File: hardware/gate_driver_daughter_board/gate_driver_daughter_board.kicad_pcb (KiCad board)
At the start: 2 copper layers, 0 parts

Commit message: PCBrev1
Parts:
- added C1: 1000uF, gate_driver_daughter_board:25V1000uF, F.Cu at (115.9, 39.3)
- added C10: 1uF, Capacitor_SMD:C_0805_2012Metric_Pad1.18x1.45mm_HandSolder, F.Cu at (156.0, 117.3)
- added C11: 0.1uF, Capacitor_SMD:C_0805_2012Metric_Pad1.18x1.45mm_HandSolder, F.Cu at (114.1, 83.7)
- added C12: 100nF, Capacitor_SMD:C_0805_2012Metric_Pad1.18x1.45mm_HandSolder, F.Cu at (173.2, 116.6)
- added C13: 10uF, Capacitor_SMD:C_0805_2012Metric_Pad1.18x1.45mm_HandSolder, F.Cu at (170.7, 116.6)
- added C14: 1000uF, gate_driver_daughter_board:25V1000uF, F.Cu at (172.8, 44.9)
- added C15: 0.1uF, Capacitor_SMD:C_0805_2012Metric_Pad1.18x1.45mm_HandSolder, F.Cu at (128.5, 81.3)
- added C16: 1000uF, gate_driver_daughter_board:25V1000uF, F.Cu at (150.6, 37.1)
- added C17: 1000uF, gate_driver_daughter_board:25V1000uF, F.Cu at (161.6, 44.9)
- added C18: 0.33uF, Capacitor_SMD:C_0805_2012Metric_Pad1.18x1.45mm_HandSolder, F.Cu at (154.9, 51.1)
- added C19: 10uF, Capacitor_SMD:C_0805_2012Metric_Pad1.18x1.45mm_HandSolder, F.Cu at (149.9, 45.2)
- added C2: 0.1uF, Capacitor_SMD:C_0805_2012Metric_Pad1.18x1.45mm_HandSolder, F.Cu at (106.7, 51.8)
- added C20: 1uF, Capacitor_SMD:C_0805_2012Metric_Pad1.18x1.45mm_HandSolder, F.Cu at (152.5, 45.2)
- added C21: 100nF, Capacitor_SMD:C_0805_2012Metric_Pad1.18x1.45mm_HandSolder, F.Cu at (155.0, 45.2)
- added C22: 0.1uF, Capacitor_SMD:C_0805_2012Metric_Pad1.18x1.45mm_HandSolder, F.Cu at (154.9, 56.1)
- added C23: 0.1uF, Capacitor_SMD:C_0805_2012Metric_Pad1.18x1.45mm_HandSolder, F.Cu at (138.2, 80.8)
- added C24: 10nF, Capacitor_SMD:C_0805_2012Metric_Pad1.18x1.45mm_HandSolder, F.Cu at (149.4, 86.4)
- added C25: 47nF, Capacitor_SMD:C_0805_2012Metric_Pad1.18x1.45mm_HandSolder, F.Cu at (154.4, 84.3)
- added C26: 0.1uF, Capacitor_SMD:C_0805_2012Metric_Pad1.18x1.45mm_HandSolder, F.Cu at (155.4, 76.7)
- added C27: 0.33uF, Capacitor_SMD:C_0805_2012Metric_Pad1.18x1.45mm_HandSolder, F.Cu at (114.8, 51.8)
- added C28: 0.1uF, Capacitor_SMD:C_0805_2012Metric_Pad1.18x1.45mm_HandSolder, F.Cu at (114.8, 55.9)
- added C3: 1000uF, gate_driver_daughter_board:25V1000uF, F.Cu at (104.7, 39.3)
- added C4: 1000uF, gate_driver_daughter_board:25V1000uF, F.Cu at (104.6, 33.3)
- added C5: 2.2uF, Capacitor_SMD:C_0805_2012Metric_Pad1.18x1.45mm_HandSolder, F.Cu at (106.7, 55.9)
- added C6: 10uF, Capacitor_SMD:C_0805_2012Metric_Pad1.18x1.45mm_HandSolder, F.Cu at (117.4, 33.5)
- added C7: 1uF, Capacitor_SMD:C_0805_2012Metric_Pad1.18x1.45mm_HandSolder, F.Cu at (114.9, 33.5)
- added C8: 100nF, Capacitor_SMD:C_0805_2012Metric_Pad1.18x1.45mm_HandSolder, F.Cu at (120.0, 33.5)
- added C9: 100nF, Capacitor_SMD:C_0805_2012Metric_Pad1.18x1.45mm_HandSolder, F.Cu at (153.4, 117.3)
- added H1: GATE, gate_driver_daughter_board:MountingHole_4.3x6.2mm_M4_Pad, F.Cu at (189.0, 115.4)
- added H2: EMITTER, gate_driver_daughter_board:MountingHole_4.3x6.2mm_M4_Pad, F.Cu at (176.0, 75.6)
- added J1: Conn_01x08, Connector_Molex:Molex_Nano-Fit_105309-xx08_1x08_P2.50mm_Vertical, F.Cu at (105.1, 76.8)
- added J2: Conn_01x02, Connector_Molex:Molex_Nano-Fit_105309-xx02_1x02_P2.50mm_Vertical, F.Cu at (152.6, 65.7)
- added J3: Conn_01x02, Connector_Molex:Molex_Nano-Fit_105309-xx02_1x02_P2.50mm_Vertical, F.Cu at (105.1, 99.8)
- added JP1: Jumper_2_Small_Open, Connector_PinHeader_2.54mm:PinHeader_1x02_P2.54mm_Vertical, F.Cu at (175.3, 107.2)
- added JP2: Jumper_2_Small_Open, Connector_PinHeader_2.54mm:PinHeader_1x02_P2.54mm_Vertical, F.Cu at (181.4, 109.7)
- added R1: R?, Resistor_SMD:R_1206_3216Metric_Pad1.30x1.75mm_HandSolder, F.Cu at (153.4, 109.2)
- added R10: 1k, Resistor_SMD:R_0805_2012Metric_Pad1.20x1.40mm_HandSolder, F.Cu at (138.2, 84.8)
- added R11: 154k, Resistor_SMD:R_0805_2012Metric_Pad1.20x1.40mm_HandSolder, F.Cu at (141.2, 74.2)
- added R12: 10k, Resistor_SMD:R_0805_2012Metric_Pad1.20x1.40mm_HandSolder, F.Cu at (137.7, 73.2)
- added R13: 8.87k, Resistor_SMD:R_0805_2012Metric_Pad1.20x1.40mm_HandSolder, F.Cu at (137.7, 75.2)
- added R14: 8.2k, Resistor_SMD:R_0805_2012Metric_Pad1.20x1.40mm_HandSolder, F.Cu at (151.9, 84.3)
- added R15: 6.8k, Resistor_SMD:R_0805_2012Metric_Pad1.20x1.40mm_HandSolder, F.Cu at (149.4, 82.3)
- added R16: 6.8k, Resistor_SMD:R_0805_2012Metric_Pad1.20x1.40mm_HandSolder, F.Cu at (151.9, 80.3)
- added R17: 10k, Resistor_SMD:R_0805_2012Metric_Pad1.20x1.40mm_HandSolder, F.Cu at (145.3, 75.2)
- added R18: 10k, Resistor_SMD:R_0805_2012Metric_Pad1.20x1.40mm_HandSolder, F.Cu at (145.3, 73.2)
- added R19: 100k, Resistor_SMD:R_0805_2012Metric_Pad1.20x1.40mm_HandSolder, F.Cu at (145.3, 115.3)
- added R3: 2.2k, Resistor_SMD:R_0805_2012Metric_Pad1.20x1.40mm_HandSolder, F.Cu at (114.6, 80.1)
- added R4: 360, Resistor_SMD:R_0805_2012Metric_Pad1.20x1.40mm_HandSolder, F.Cu at (128.5, 83.8)
- added R5: 102k, Resistor_SMD:R_0805_2012Metric_Pad1.20x1.40mm_HandSolder, F.Cu at (128.5, 78.7)
- added R6: 976k, Resistor_SMD:R_0805_2012Metric_Pad1.20x1.40mm_HandSolder, F.Cu at (130.6, 75.9)
- added R7: 130k 0.5%, Resistor_SMD:R_0805_2012Metric_Pad1.20x1.40mm_HandSolder, F.Cu at (133.6, 78.2)
- added R8: R?, Resistor_SMD:R_1206_3216Metric_Pad1.30x1.75mm_HandSolder, F.Cu at (179.8, 116.3)
- added R9: R?, Resistor_SMD:R_1206_3216Metric_Pad1.30x1.75mm_HandSolder, F.Cu at (179.8, 113.3)
- added Rg1: 549, Resistor_SMD:R_0805_2012Metric_Pad1.20x1.40mm_HandSolder, F.Cu at (151.4, 69.1)
- added TP1: InAmp_Bias/Amp, TestPoint:TestPoint_Pad_D3.0mm, F.Cu at (141.2, 88.4)
- added TP2: InAmp_Filtered, TestPoint:TestPoint_Pad_D3.0mm, F.Cu at (145.8, 88.4)
- added TP3: InAmpOut, TestPoint:TestPoint_Pad_2.0x2.0mm, F.Cu at (154.7, 80.5)
- added U1: LF33_TO220, Package_TO_SOT_THT:TO-220-3_Vertical, F.Cu at (109.8, 50.8)
- added U2: REC20K-2412SZ, gate_driver_daughter_board:REC20K_RCP, F.Cu at (124.4, 36.6)
- added U3: 6N137, Package_DIP:DIP-8_W7.62mm, F.Cu at (125.0, 86.2)
- added U4: NCD57100DWR2G, Package_SO:SOIC-16W_7.5x10.3mm_P1.27mm, F.Cu at (163.1, 112.4)
- added U5: LTC6992CS6-2-TRMPBF, Package_TO_SOT_SMD:TSOT-23-6, F.Cu at (133.6, 81.3)
- added U6: LM7805_TO220, Package_TO_SOT_THT:TO-220-3_Vertical, F.Cu at (149.9, 50.5)
- added U7: MCP6004, Package_SO:SOIC-14_3.9x8.7mm_P1.27mm, F.Cu at (143.8, 81.3)
- added U8: INA826, Package_SO:SOIC-8_3.9x4.9mm_P1.27mm, F.Cu at (151.3, 74.2)
- added U9: LM7805_TO220, Package_TO_SOT_THT:TO-220-3_Vertical, F.Cu at (117.9, 50.8)
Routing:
- net +15V_Isolated: track 0.00 -> 134.1 mm
- net +12V: track 0.00 -> 123.2 mm
- net +5V_Isolated: track 0.00 -> 106.2 mm
- net +3.3V: track 0.00 -> 100.3 mm, vias 0 -> 4
- net /~{Rp_GD_ResetFinal}: track 0.00 -> 87.1 mm
- net /Rp_GD_Ready: track 0.00 -> 63.6 mm
- net /~{Rp_GD_Fault}: track 0.00 -> 63.2 mm
- net /Rb_GateDrive: track 0.00 -> 57.0 mm
- net +5V: track 0.00 -> 37.2 mm, vias 0 -> 1
- net Net-(JP2-A): track 0.00 -> 26.8 mm
- net Net-(U7B--): track 0.00 -> 23.9 mm, vias 0 -> 2
- net Net-(U7B-+): track 0.00 -> 16.6 mm
- net Net-(U5-MOD): track 0.00 -> 14.4 mm
- net /Rp_CurrentSense: track 0.00 -> 12.6 mm
- net Net-(U4-OUTH): track 0.00 -> 11.9 mm
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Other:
- board outline added: 103.9 x 116.8 mm

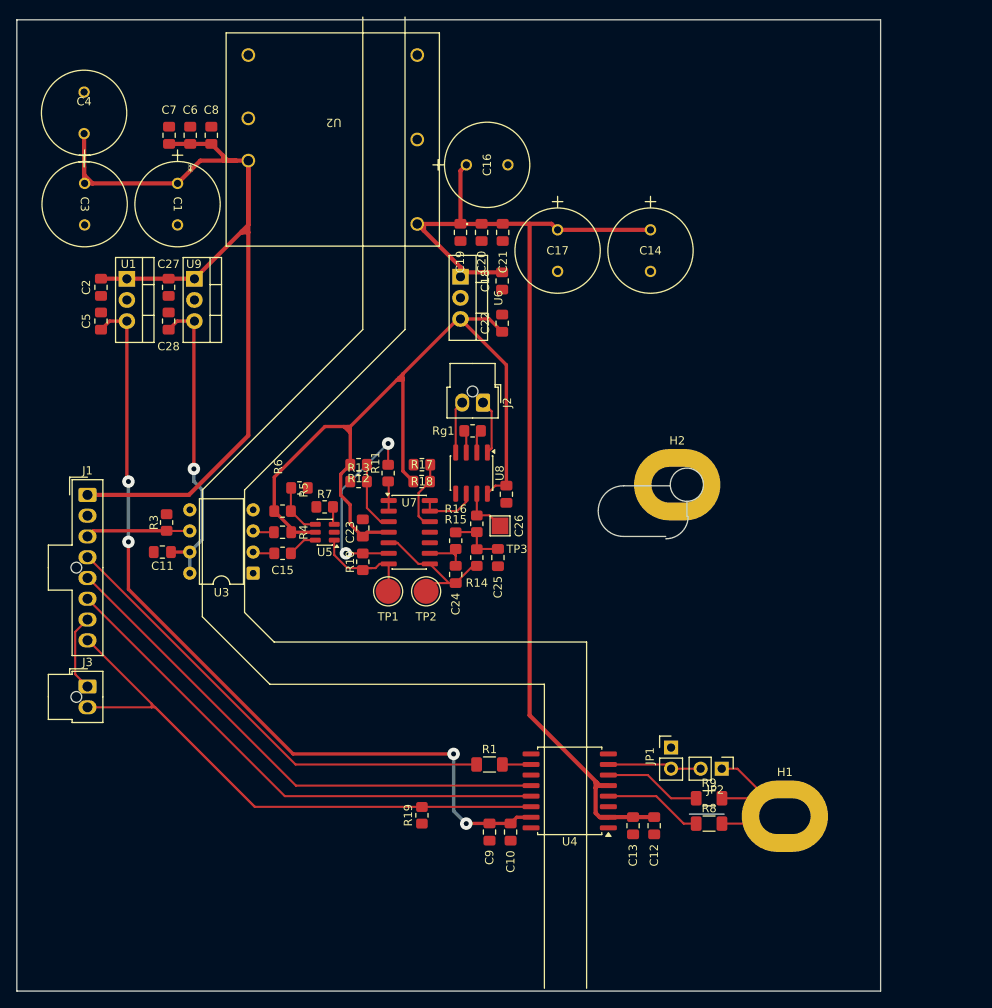
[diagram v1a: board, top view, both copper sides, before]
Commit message: Add Isolation Keepout Zone, little bit of ground routing
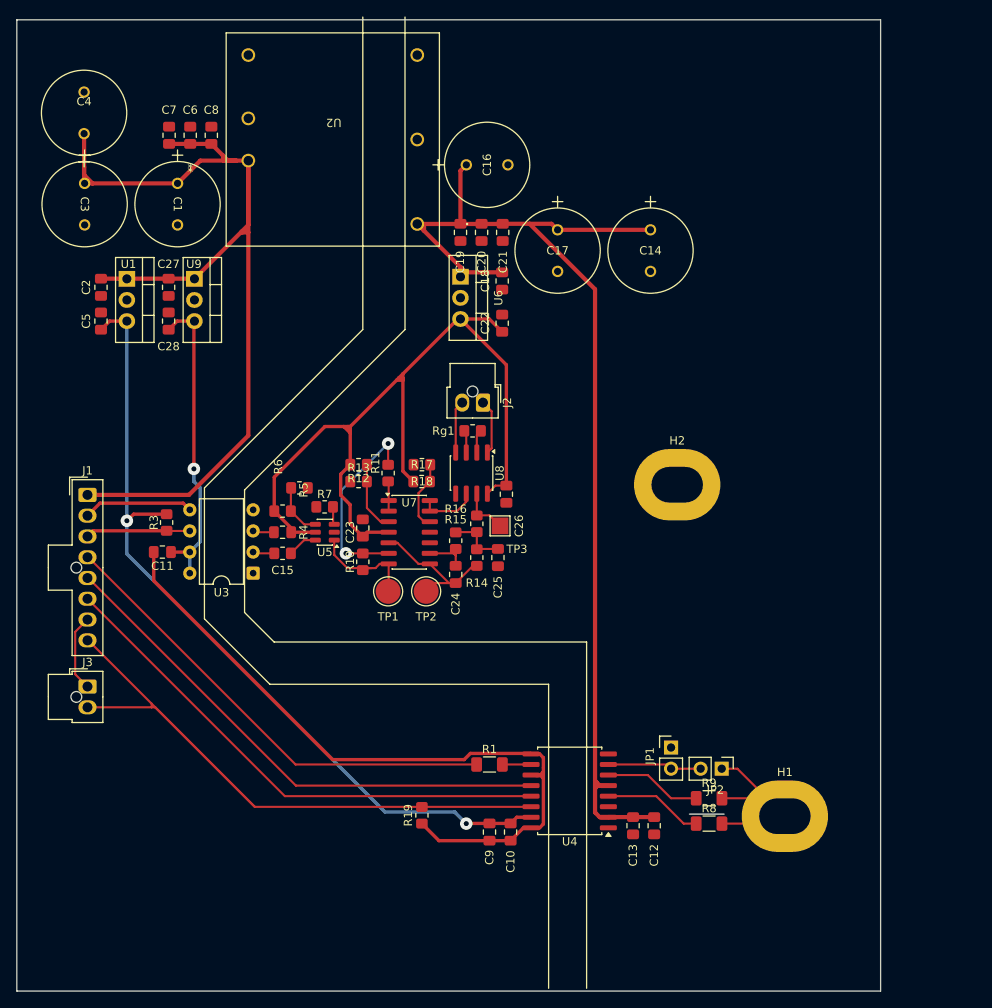
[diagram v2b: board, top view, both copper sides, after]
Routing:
- net GND: track 0.00 -> 100.7 mm
- net +3.3V: track 100.3 -> 99.2 mm, vias 4 -> 2
- net +15V_Isolated: track 134.1 -> 134.9 mm
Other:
- outline, holes or cut-outs redrawn

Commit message: Annular Ring Adjustment
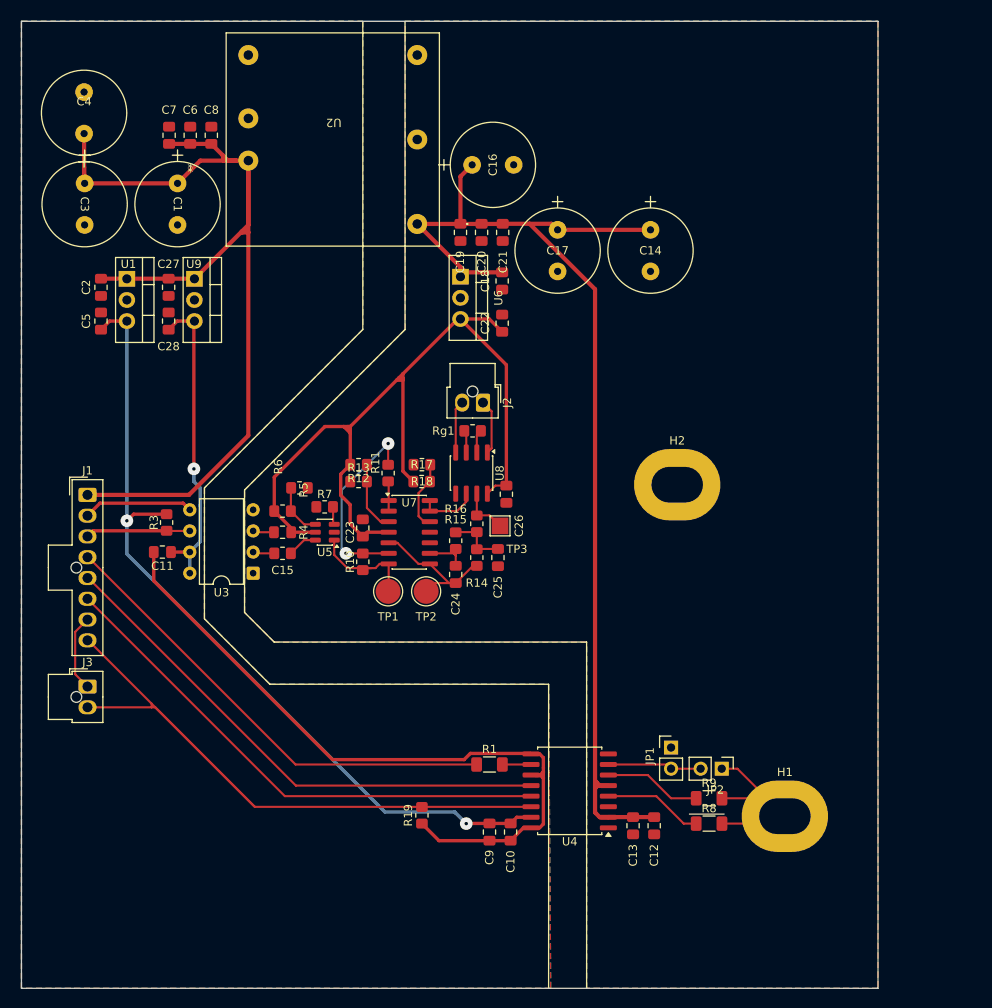
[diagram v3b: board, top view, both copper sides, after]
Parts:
- moved C16 0.70 mm to (151.3, 37.1)
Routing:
- added copper zone on B.Cu, net Battery-
- added copper zone on F.Cu, net Battery-
- added copper zone on B.Cu, net GND
- added copper zone on F.Cu, net GND
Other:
- board size 103.9 x 116.8 mm -> 103 x 116.3 mm
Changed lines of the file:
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@@
 		(pad "1" thru_hole circle
 			(at 0 0 180)
-			(size 1.651 1.651)
+			(size 2.413 1.651)
 			(drill 1.143)
 			(layers "*.Cu" "*.Mask")
@@
 		(pad "2" thru_hole circle
 			(at 0 5.08 180)
-			(size 1.651 1.651)
+			(size 2.413 1.651)
 			(drill 1.143)
 			(layers "*.Cu" "*.Mask")
@@
 		(pad "3" thru_hole circle
 			(at 0 12.7 180)
-			(size 1.651 1.651)
+			(size 2.413 1.651)
 			(drill 1.143)
 			(layers "*.Cu" "*.Mask")
@@
 		(pad "4" thru_hole circle
 			(at -20.32 12.7 180)
-			(size 1.651 1.651)
+			(size 2.413 1.651)
 			(drill 1.143)
 			(layers "*.Cu" "*.Mask")
@@
 		(pad "5" thru_hole circle
 			(at -20.32 2.54 180)
-			(size 1.651 1.651)
+			(size 2.413 2.413)
 			(drill 1.143)
 			(layers "*.Cu" "*.Mask")
@@
 		(pad "6" thru_hole circle
 			(at -20.32 -7.62 180)
-			(size 1.651 1.651)
+			(size 2.413 1.651)
 			(drill 1.143)
 			(layers "*.Cu" "*.Mask")
@@
 	(footprint "gate_driver_daughter_board:25V1000uF"
 		(layer "F.Cu")
-		(at 150.63275 37.084)
+		(at 151.32875 37.084)
 		(tags "UVY1E102MPD1TD ")
 		(property "Reference" "C16"
@@
 		(pad "1" thru_hole circle
 			(at 0 0)
-			(size 1.3716 1.3716)
+			(size 2.1336 2.1336)
 			(drill 0.8636)
 			(layers "*.Cu" "*.Mask")
@@
 		(pad "2" thru_hole circle
 			(at 5 0)
-			(size 1.3716 1.3716)
+			(size 2.1336 1.3716)
 			(drill 0.8636)
 			(layers "*.Cu" "*.Mask")
@@
 		(pad "1" thru_hole circle
 			(at 0 0 90)
-			(size 1.3716 1.3716)
+			(size 2.1336 1.3716)
 			(drill 0.8636)
 			(layers "*.Cu" "*.Mask")
@@
 		(pad "2" thru_hole circle
 			(at 5 0 90)
-			(size 1.3716 1.3716)
+			(size 2.1336 1.3716)
 			(drill 0.8636)
 			(layers "*.Cu" "*.Mask")
@@
 		(pad "1" thru_hole circle
 			(at 0 0 270)
-			(size 1.3716 1.3716)
+			(size 2.1336 1.3716)
 			(drill 0.8636)
 			(layers "*.Cu" "*.Mask")
@@
 		(pad "2" thru_hole circle
 			(at 5 0 270)
-			(size 1.3716 1.3716)
+			(size 2.1336 1.3716)
 			(drill 0.8636)
 			(layers "*.Cu" "*.Mask")
@@
 		(pad "1" thru_hole circle
 			(at 0 0 270)
-			(size 1.3716 1.3716)
+			(size 2.1336 1.3716)
 			(drill 0.8636)
 			(layers "*.Cu" "*.Mask")
@@
 		(pad "2" thru_hole circle
 			(at 5 0 270)
-			(size 1.3716 1.3716)
+			(size 2.1336 1.3716)
 			(drill 0.8636)
 			(layers "*.Cu" "*.Mask")
@@
 		(pad "1" thru_hole circle
 			(at 0 0 270)
-			(size 1.3716 1.3716)
+			(size 2.1336 1.3716)
 			(drill 0.8636)
 			(layers "*.Cu" "*.Mask")
@@
 		(pad "2" thru_hole circle
 			(at 5 0 270)
-			(size 1.3716 1.3716)
+			(size 2.1336 1.3716)
 			(drill 0.8636)
 			(layers "*.Cu" "*.Mask")
@@
 		(pad "1" thru_hole circle
 			(at 0 0 270)
-			(size 1.3716 1.3716)
+			(size 2.1336 1.3716)
 			(drill 0.8636)
 			(layers "*.Cu" "*.Mask")
@@
 		(pad "2" thru_hole circle
 			(at 5 0 270)
-			(size 1.3716 1.3716)
+			(size 2.1336 1.3716)
 			(drill 0.8636)
 			(layers "*.Cu" "*.Mask")
@@
 	)
 	(gr_line
-		(start 138.176 19.304)
+		(start 138.176 19.812)
 		(end 138.176 56.896)
 		(stroke
@@
 	(gr_line
 		(start 143.256 56.896)
-		(end 143.256 19.304)
+		(end 143.256 19.812)
 		(stroke
 			(width 0.1)
@@
 	)
 	(gr_rect
-		(start 96.557401 19.637365)
-		(end 200.467717 136.477364)
+		(start 97.111468 19.812)
+		(end 200.152 136.143999)
 		(stroke
 			(width 0.05)
@@
 	(via
 		(at 117.856 73.66)
-		(size 1.50114)
-		(drill 0.59944)
+		(size 1.524)
+		(drill 0.4064)
 		(layers "F.Cu" "B.Cu")
 		(net "+5V")
@@
 	(via
 		(at 136.144 83.82)
-		(size 1.50114)
-		(drill 0.59944)
+		(size 1.524)
+		(drill 0.4064)
 		(layers "F.Cu" "B.Cu")
 		(net "Net-(U7B--)")
@@
 	(via
 		(at 141.224 70.612)
-		(size 1.503223)
-		(drill 0.59944)
+		(size 1.524)
+		(drill 0.4064)
 		(layers "F.Cu" "B.Cu")
 		(net "Net-(U7B--)")
@@
 	)
 	(segment
+		(start 149.926 38.48675)
+		(end 151.32875 37.084)
+		(width 0.508)
+		(layer "F.Cu")
+		(net "+15V_Isolated")
+	)
+	(segment
 		(start 166.2775 111.3445)
 		(end 166.116 111.183)
@@
 	)
 	(segment
-		(start 166.439 111.76)
-		(end 166.185 112.014)
+		(start 149.926 44.1745)
+		(end 149.926 38.48675)
 		(width 0.508)
 		(layer "F.Cu")
@@
 	)
 	(segment
-		(start 155.006 44.1745)
-		(end 158.242 44.1745)
-		(width 0.508)
-		(layer "F.Cu")
-		(net "+15V_Isolated")
-	)
-	(segment
-		(start 149.926 37.79075)
-		(end 149.926 44.1745)
+		(start 166.439 111.76)
+		(end 166.185 112.014)
 		(width 0.508)
 		(layer "F.Cu")
@@
 	)
 	(segment
-		(start 150.63275 37.084)
-		(end 149.926 37.79075)
+		(start 155.006 44.1745)
+		(end 158.242 44.1745)
 		(width 0.508)
 		(layer "F.Cu")
@@
 	(via
 		(at 109.794 79.90123)
-		(size 1.50114)
-		(drill 0.59944)
+		(size 1.524)
+		(drill 0.4064)
 		(layers "F.Cu" "B.Cu")
 		(net "+3.3V")
@@
 	(via
 		(at 150.622 116.332)
-		(size 1.50114)
-		(drill 0.59944)
+		(size 1.524)
+		(drill 0.4064)
 		(layers "F.Cu" "B.Cu")
 		(net "+3.3V")
@@
 		(polygon
 			(pts
-				(xy 138.176 19.558) (xy 143.256 19.558) (xy 143.256 56.896) (xy 123.952 76.2) (xy 123.952 90.932)
-				(xy 127.508 94.488) (xy 165.1 94.488) (xy 165.1 136.652) (xy 160.528 136.652) (xy 160.528 99.568)
+				(xy 138.176 19.812) (xy 143.256 19.812) (xy 143.256 56.896) (xy 123.952 76.2) (xy 123.952 90.932)
+				(xy 127.508 94.488) (xy 165.1 94.488) (xy 165.1 136.144) (xy 160.528 136.144) (xy 160.528 99.568)
 				(xy 127 99.568) (xy 119.126 91.694) (xy 119.126 75.946) (xy 138.176 56.896)
 			)
 		)
+	)
+	(zone
+		(net "GND")
+		(layers "F.Cu" "B.Cu")
+		(name "GND")
+		(hatch edge 0.5)
+		(priority 1)
+		(connect_pads yes
+			(clearance 0.4064)
+		)
+		(min_thickness 0.25)
+		(fill yes
+			(thermal_gap 0.5)
+			(thermal_bridge_width 0.5)
+			(island_removal_mode 0)
+		)
+		(polygon
+			(pts
+				(xy 97.111468 19.812) (xy 138.176 19.812) (xy 138.176 56.896) (xy 119.126 75.946) (xy 119.126 91.694)
+				(xy 127 99.568) (xy 160.528 99.568) (xy 160.782 136.144) (xy 97.111468 136.143999)
+			)
+		)
+	)
+	(zone
+		(net "Battery-")
+		(layers "F.Cu" "B.Cu")
+		(name "Bat-")
+		(hatch edge 0.5)
+		(connect_pads yes
+			(clearance 0.4064)
+		)
+		(min_thickness 0.25)
+		(fill yes
+			(thermal_gap 0.5)
+			(thermal_bridge_width 0.5)
+			(island_removal_mode 0)
+		)
+		(polygon
+			(pts
+				(xy 143.256 19.812) (xy 200.152 19.812) (xy 200.152 136.143999) (xy 165.1 136.144) (xy 165.1 94.488)
+				(xy 127.508 94.488) (xy 123.952 90.932) (xy 123.952 76.2) (xy 143.256 56.896)
+			)
+		)

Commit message: V1.0 PCB Ready to Mill, Gate Driver Daughter Board
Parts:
- moved R13 1.59 mm to (138.9, 74.2), turned to -90 degrees
- moved C12 1.55 mm to (173.0, 118.1)
- moved C13 1.55 mm to (170.4, 118.1)
- moved R12 1.44 mm to (136.7, 74.2), turned to 90 degrees
- moved R7 1.00 mm to (132.6, 78.2)
- turned C23 to 90 degrees
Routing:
- net GND: track 100.7 -> 87.4 mm
- net Battery-: track 2.35 -> 10.1 mm, vias 0 -> 4
- net Net-(U7D--): track 7.09 -> 8.65 mm
- net +5V_Isolated: track 106.2 -> 105.3 mm
- net +12V: track 123.2 -> 122.6 mm
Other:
- outline, holes or cut-outs redrawn
